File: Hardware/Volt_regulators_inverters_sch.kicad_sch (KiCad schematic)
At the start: 18 parts, among them J6 dvdd_test, J7 -2.5v_test, J8 -2.5v_reg_test, J9 2.5v_reg_test, U11 LM2665M6, U6 TPS73133DBV, U7 TPS72325DBV, U8 TLV70310DBVR

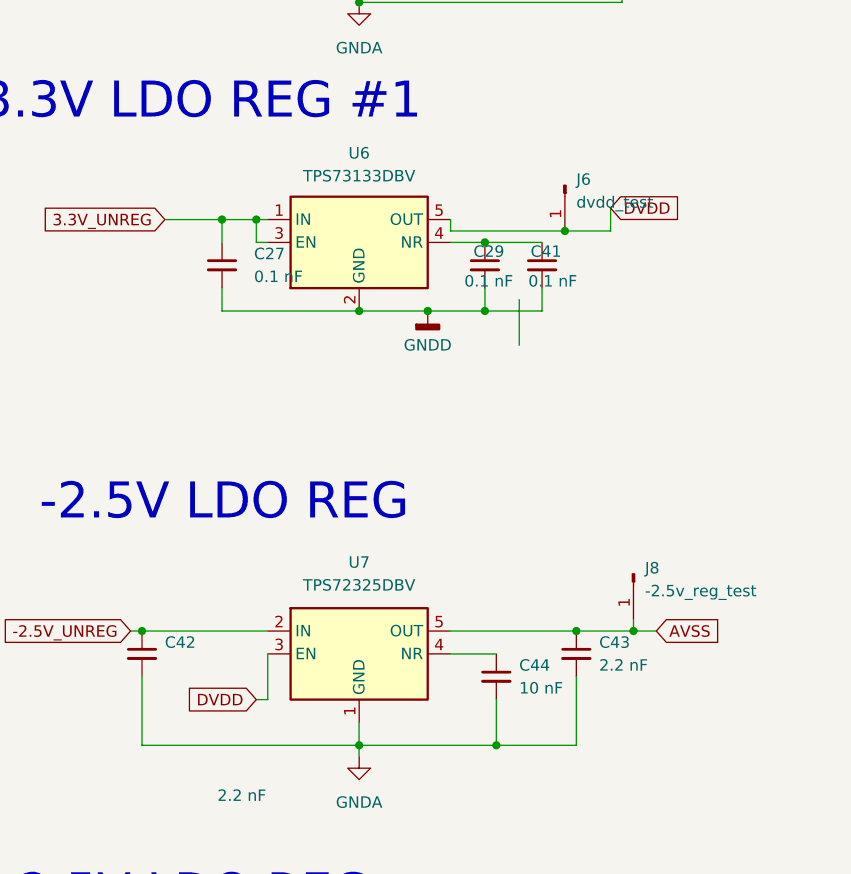
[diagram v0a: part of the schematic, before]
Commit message: feat:begin rev3 with rp2350
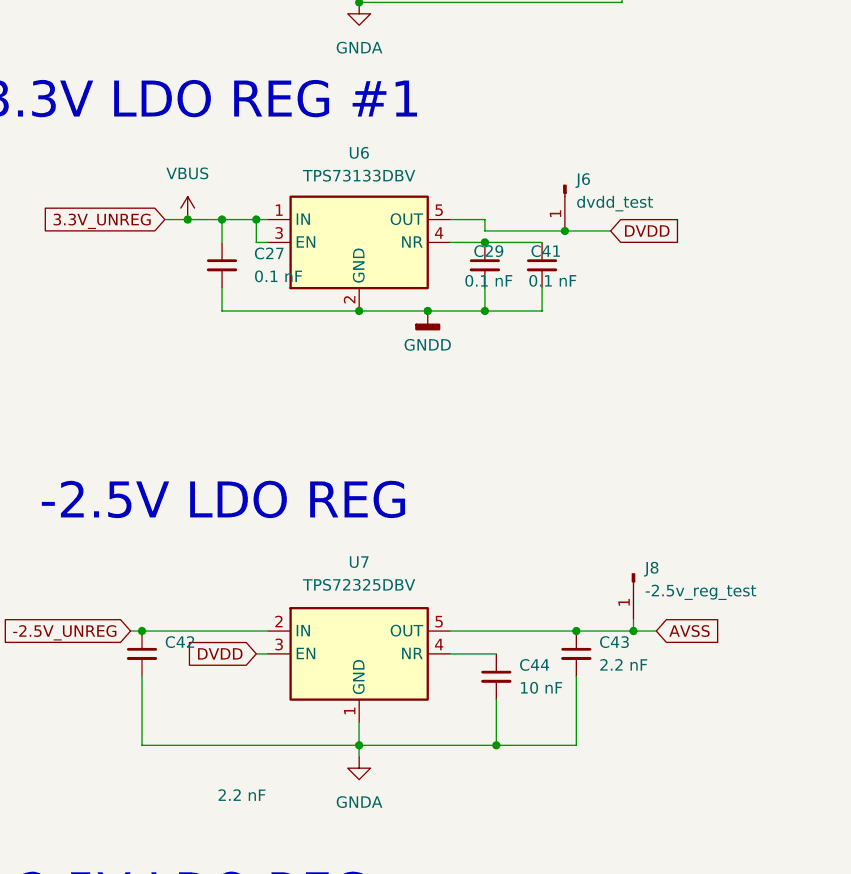
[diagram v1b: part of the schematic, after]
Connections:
- net 3.3V_UNREG renamed VBUS
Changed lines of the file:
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@@
+	)
+	(junction
+		(at 41.91 72.39)
+		(diameter 0)
+		(color 0 0 0 0)
 	)
 	(junction
@@
 	(wire
 		(pts
-			(xy 71.12 73.66) (xy 71.12 72.39)
+			(xy 74.93 73.66) (xy 74.93 72.39)
 		)
 		(stroke
@@
 	(wire
 		(pts
-			(xy 88.9 73.66) (xy 83.82 73.66)
-		)
-		(stroke
-			(width 0)
-			(type default)
-		)
-	)
-	(wire
-		(pts
 			(xy 93.98 38.1) (xy 91.44 38.1)
 		)
@@
 	(wire
 		(pts
-			(xy 39.37 72.39) (xy 45.72 72.39)
+			(xy 83.82 73.66) (xy 74.93 73.66)
+		)
+		(stroke
+			(width 0)
+			(type default)
+		)
+	)
+	(wire
+		(pts
+			(xy 39.37 72.39) (xy 41.91 72.39)
 		)
 		(stroke
@@
 	(wire
 		(pts
-			(xy 50.8 125.73) (xy 50.8 120.65)
-		)
-		(stroke
-			(width 0)
-			(type default)
-		)
-	)
-	(wire
-		(pts
 			(xy 90.17 40.64) (xy 90.17 38.1)
 		)
@@
 	(wire
 		(pts
-			(xy 83.82 73.66) (xy 71.12 73.66)
-		)
-		(stroke
-			(width 0)
-			(type default)
-		)
-	)
-	(wire
-		(pts
 			(xy 39.37 172.72) (xy 39.37 168.91)
 		)
@@
 	(wire
 		(pts
-			(xy 49.53 125.73) (xy 50.8 125.73)
+			(xy 49.53 120.65) (xy 50.8 120.65)
 		)
 		(stroke
@@
 	(wire
 		(pts
-			(xy 78.74 81.28) (xy 78.74 86.36)
-		)
-		(stroke
-			(width 0)
-			(type default)
-		)
-	)
-	(wire
-		(pts
 			(xy 71.12 118.11) (xy 85.09 118.11)
 		)
@@
 	(wire
 		(pts
+			(xy 83.82 73.66) (xy 88.9 73.66)
+		)
+		(stroke
+			(width 0)
+			(type default)
+		)
+	)
+	(wire
+		(pts
 			(xy 27.94 163.83) (xy 27.94 172.72)
 		)
@@
 	(wire
 		(pts
-			(xy 88.9 71.12) (xy 88.9 73.66)
+			(xy 74.93 72.39) (xy 71.12 72.39)
+		)
+		(stroke
+			(width 0)
+			(type default)
+		)
+	)
+	(wire
+		(pts
+			(xy 41.91 72.39) (xy 45.72 72.39)
 		)
 		(stroke
@@
 	(global_label "DVDD"
 		(shape input)
-		(at 88.9 71.12 0)
+		(at 88.9 73.66 0)
 		(fields_autoplaced yes)
 		(effects
@@
 		)
 		(property "Intersheetrefs" "${INTERSHEET_REFS}"
-			(at 96.7838 71.12 0)
+			(at 96.7838 73.66 0)
 			(effects
 				(font
@@
 	(global_label "DVDD"
 		(shape input)
-		(at 49.53 125.73 180)
+		(at 49.53 120.65 180)
 		(fields_autoplaced yes)
 		(effects
@@
 		)
 		(property "Intersheetrefs" "${INTERSHEET_REFS}"
-			(at 41.6462 125.73 0)
+			(at 41.6462 120.65 0)
 			(effects
 				(font
@@
 		)
 		(instances
-			(project ""
+			(project "bioamplifier"
 				(path "/59c54cdb-19a2-4654-a4c9-f1907d038780/db58efb1-7103-4a17-b794-0e1a9c461960"
 					(reference "U7")
@@
 		)
 		(instances
-			(project ""
+			(project "bioamplifier"
 				(path "/59c54cdb-19a2-4654-a4c9-f1907d038780/db58efb1-7103-4a17-b794-0e1a9c461960"
 					(reference "U8")
+					(unit 1)
+				)
+			)
+		)
+	)
+	(symbol
+		(lib_id "power:VBUS")
+		(at 41.91 72.39 0)
+		(unit 1)
+		(exclude_from_sim no)
+		(in_bom yes)
+		(on_board yes)
+		(dnp no)
+		(fields_autoplaced yes)
+		(property "Reference" "#PWR022"
+			(at 41.91 76.2 0)
+			(effects
+				(font
+					(size 1.27 1.27)
+				)
+				(hide yes)
+			)
+		)
+		(property "Value" "VBUS"
+			(at 41.91 67.31 0)
+			(effects
+				(font
+					(size 1.27 1.27)
+				)
+			)
+		)
+		(property "Footprint" ""
+			(at 41.91 72.39 0)
+			(effects
+				(font
+					(size 1.27 1.27)
+				)
+				(hide yes)
+			)
+		)
+		(property "Datasheet" ""
+			(at 41.91 72.39 0)
+			(effects
+				(font
+					(size 1.27 1.27)
+				)
+				(hide yes)
+			)
+		)
+		(property "Description" "Power symbol creates a global label with name \"VBUS\""
+			(at 41.91 72.39 0)
+			(effects
+				(font
+					(size 1.27 1.27)
+				)
+				(hide yes)
+			)
+		)
+		(pin "1"
+		)
+		(instances
+			(project "bioamplifier"
+				(path "/59c54cdb-19a2-4654-a4c9-f1907d038780/db58efb1-7103-4a17-b794-0e1a9c461960"
+					(reference "#PWR022")
 					(unit 1)
 				)
@@
 		)
 		(instances
-			(project ""
+			(project "bioamplifier"
 				(path "/59c54cdb-19a2-4654-a4c9-f1907d038780/db58efb1-7103-4a17-b794-0e1a9c461960"
 					(reference "#PWR034")
@@
 		)
 		(instances
-			(project ""
+			(project "bioamplifier"
 				(path "/59c54cdb-19a2-4654-a4c9-f1907d038780/db58efb1-7103-4a17-b794-0e1a9c461960"
 					(reference "#PWR057")
